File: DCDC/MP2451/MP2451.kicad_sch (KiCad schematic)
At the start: 9 parts, among them U1 MP2451

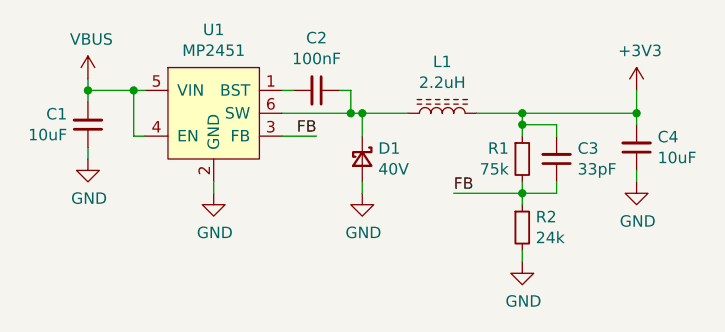
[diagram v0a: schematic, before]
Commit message: Revert "Update modules to kicad v7 format"
This reverts commit 3325eb02d48d3d222bc7f8945228a1814ae85736.
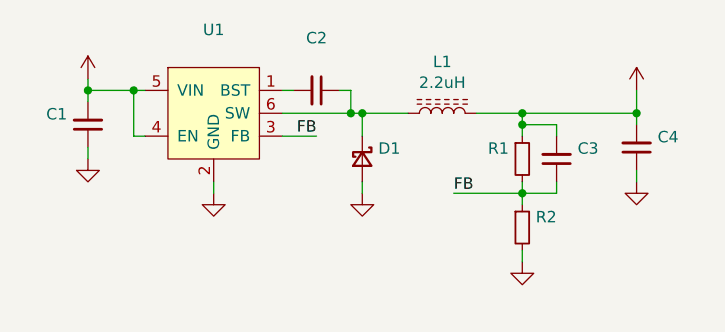
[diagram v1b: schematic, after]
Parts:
- C1: value 10uF -> (none); footprint Capacitor_SMD:C_1206_3216Metric -> (none)
- C2: value 100nF -> (none); footprint Capacitor_SMD:C_0402_1005Metric -> (none)
- C3: value 33pF -> (none); footprint Capacitor_SMD:C_0402_1005Metric -> (none)
- C4: value 10uF -> (none); footprint Capacitor_SMD:C_0402_1005Metric -> (none)
- D1: value 40V -> (none); footprint Diode_SMD:D_SOD-123 -> (none)
- R1: value 75k -> (none); footprint Resistor_SMD:R_0402_1005Metric -> (none)
- R2: value 24k -> (none); footprint Resistor_SMD:R_0402_1005Metric -> (none)
- U1: value MP2451 -> (none); footprint Package_TO_SOT_SMD:SOT-23-6 -> (none)

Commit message: Reapply "Update modules to kicad v7 format"
This reverts commit fa5cc85431189ac7a3beedf0871b5723203ae43f.
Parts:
- C1: value (none) -> 10uF; footprint (none) -> Capacitor_SMD:C_1206_3216Metric
- C2: value (none) -> 100nF; footprint (none) -> Capacitor_SMD:C_0402_1005Metric
- C3: value (none) -> 33pF; footprint (none) -> Capacitor_SMD:C_0402_1005Metric
- C4: value (none) -> 10uF; footprint (none) -> Capacitor_SMD:C_0402_1005Metric
- D1: value (none) -> 40V; footprint (none) -> Diode_SMD:D_SOD-123
- R1: value (none) -> 75k; footprint (none) -> Resistor_SMD:R_0402_1005Metric
- R2: value (none) -> 24k; footprint (none) -> Resistor_SMD:R_0402_1005Metric
- U1: value (none) -> MP2451; footprint (none) -> Package_TO_SOT_SMD:SOT-23-6
